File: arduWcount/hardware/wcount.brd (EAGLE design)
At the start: 100 x 80 mm, 25 parts, among them IC1 MEGA8-AI, Q2 BC447, Q4 BC447

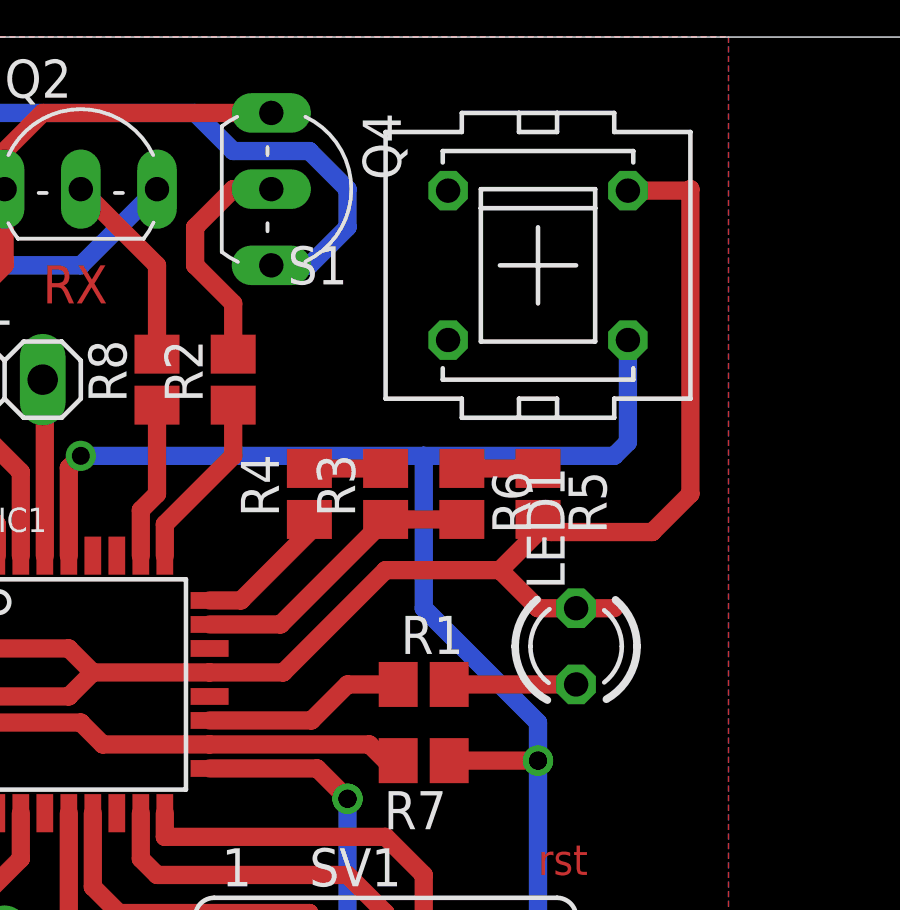
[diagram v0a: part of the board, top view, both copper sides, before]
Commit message: EEPROM rotating added
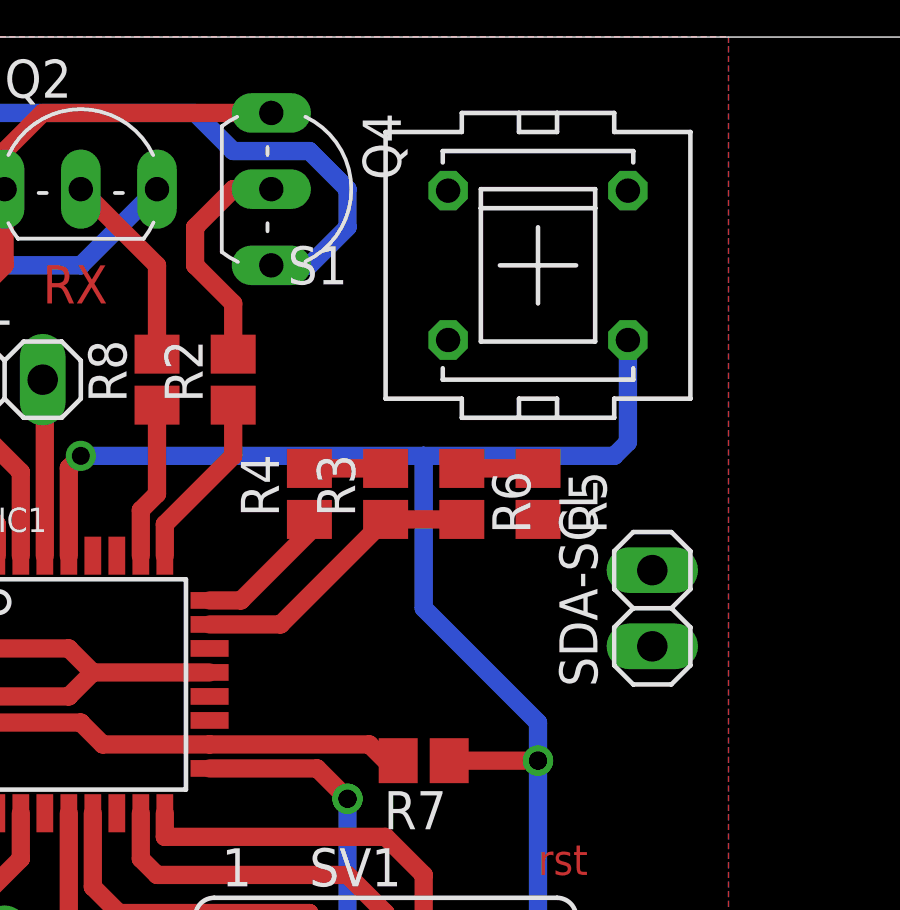
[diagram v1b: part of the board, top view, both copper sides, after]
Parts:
- removed LED1: (no value), led:LED3MM
- removed R1: (no value), resistor:R0805
- added SDA-SCL: (no value), pinhead:1X02
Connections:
- net GNDA: no longer LED1.K
- net N$22: now also IC1.27, SDA-SCL.1; no longer LED1.A, R1.2
- net N$23: now also IC1.28, SDA-SCL.2; no longer IC1.19, R1.1
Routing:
- net GNDA: track 151.3 -> 116.1 mm
- net N$23: track 6.78 -> 0.00 mm
- net N$22: track 4.23 -> 0.00 mm
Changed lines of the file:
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@@
 <attribute name="SPICEPREFIX" value="C" x="-13.97" y="116.84" size="1.778" layer="27" rot="R180" display="off"/>
 </element>
-<element name="LED1" library="led" package="LED3MM" value="" x="39.37" y="59.69" rot="R90"/>
-<element name="R1" library="resistor" package="R0805" value="" x="34.29" y="58.42"/>
 <element name="R5" library="resistor" package="R0805" value="" x="38.1" y="64.77" rot="R270"/>
 <element name="R6" library="resistor" package="R0805" value="" x="35.56" y="64.77" rot="R270"/>
@@
 </element>
 <element name="C5" library="resistor" package="C0805" value="0.1 mf" x="40.64" y="48.26" rot="R270"/>
+<element name="SDA-SCL" library="pinhead" package="1X02" value="" x="41.91" y="60.96" rot="R90"/>
 </elements>
 <signals>
@@
 <via x="38.1" y="55.88" extent="1-16" drill="0.6" diameter="0.8128"/>
 <contactref element="C5" pad="1"/>
-<wire x1="22.86" y1="66.04" x2="22.86" y2="66.04" width="0" layer="19" extent="1-16"/>
 <wire x1="38.1" y1="49.53" x2="40.64" y2="49.53" width="0.6096" layer="1"/>
 <wire x1="40.64" y1="49.53" x2="40.64" y2="49.11" width="0.6096" layer="1"/>
-</signal>
-<signal name="N$22">
-<contactref element="LED1" pad="A"/>
-<contactref element="R1" pad="2"/>
-<wire x1="35.14" y1="58.42" x2="39.37" y2="58.42" width="0.6096" layer="1"/>
-</signal>
-<signal name="N$23">
-<contactref element="IC1" pad="19"/>
-<contactref element="R1" pad="1"/>
-<wire x1="27.1526" y1="57.22" x2="30.55" y2="57.22" width="0.6096" layer="1"/>
-<wire x1="30.55" y1="57.22" x2="31.75" y2="58.42" width="0.6096" layer="1"/>
-<wire x1="31.75" y1="58.42" x2="33.44" y2="58.42" width="0.6096" layer="1"/>
+<wire x1="22.86" y1="66.04" x2="22.86" y2="66.04" width="0" layer="19" extent="1-16"/>
 </signal>
 <signal name="N$25">
@@
 <contactref element="SV1" pad="2"/>
 <contactref element="R5" pad="2"/>
-<contactref element="LED1" pad="K"/>
 <contactref element="VALTEC" pad="2"/>
 <contactref element="PWR" pad="1"/>
@@
 <wire x1="23.26" y1="58.82" x2="22.46" y2="58.02" width="0.6096" layer="1"/>
 <wire x1="22.46" y1="58.02" x2="18.5674" y2="58.02" width="0.6096" layer="1"/>
-<wire x1="27.1526" y1="58.82" x2="29.61" y2="58.82" width="0.6096" layer="1"/>
-<wire x1="29.61" y1="58.82" x2="33.02" y2="62.23" width="0.6096" layer="1"/>
-<wire x1="33.02" y1="62.23" x2="36.83" y2="62.23" width="0.6096" layer="1"/>
-<wire x1="36.83" y1="62.23" x2="38.1" y2="63.5" width="0.6096" layer="1"/>
-<wire x1="39.37" y1="60.96" x2="38.1" y2="60.96" width="0.6096" layer="1"/>
-<wire x1="38.1" y1="60.96" x2="36.83" y2="62.23" width="0.6096" layer="1"/>
 <wire x1="20.32" y1="49.53" x2="20.32" y2="46.99" width="0.6096" layer="1"/>
 <wire x1="20.32" y1="46.99" x2="2.54" y2="46.99" width="0.6096" layer="1"/>
@@
 <wire x1="2.54" y1="50.48" x2="2.86" y2="50.8" width="0.6096" layer="1"/>
 <wire x1="27.94" y1="46.99" x2="20.32" y2="46.99" width="0.6096" layer="1"/>
-<wire x1="41.0972" y1="74.8792" x2="43.1292" y2="74.8792" width="0.6096" layer="1"/>
-<wire x1="43.1292" y1="74.8792" x2="43.18" y2="74.93" width="0.6096" layer="1"/>
-<wire x1="43.18" y1="74.93" x2="43.18" y2="64.77" width="0.6096" layer="1"/>
-<wire x1="43.18" y1="64.77" x2="41.91" y2="63.5" width="0.6096" layer="1"/>
-<wire x1="41.91" y1="63.5" x2="38.52" y2="63.5" width="0.6096" layer="1"/>
-<wire x1="38.52" y1="63.5" x2="38.1" y2="63.92" width="0.6096" layer="1"/>
 <wire x1="2.54" y1="59.69" x2="1.27" y2="60.96" width="0.6096" layer="1"/>
 <wire x1="1.27" y1="60.96" x2="1.27" y2="67.31" width="0.6096" layer="1"/>
@@
 <wire x1="18.5674" y1="59.62" x2="22.46" y2="59.62" width="0.6096" layer="1"/>
 <wire x1="22.46" y1="59.62" x2="23.26" y2="58.82" width="0.6096" layer="1"/>
-<wire x1="39.37" y1="60.96" x2="40.64" y2="60.96" width="0.6096" layer="1"/>
 <polygon width="0.6096" layer="1" isolate="0.8128">
 <vertex x="0" y="80.01"/>
@@
 <vertex x="0" y="41.91"/>
 </polygon>
+<wire x1="41.0972" y1="74.8792" x2="38.1" y2="63.92" width="0" layer="19" extent="1-1"/>
+<wire x1="27.1526" y1="58.82" x2="38.1" y2="63.92" width="0" layer="19" extent="1-1"/>
 </signal>
 <signal name="N$16">
@@
 <wire x1="38.1" y1="47.41" x2="38.1" y2="46.99" width="0.6096" layer="1"/>
 </signal>
+<signal name="N$22">
+<contactref element="IC1" pad="27"/>
+<contactref element="SDA-SCL" pad="1"/>
+<wire x1="24.06" y1="62.7126" x2="41.91" y2="59.69" width="0" layer="19" extent="1-1"/>
+</signal>
+<signal name="N$23">
+<contactref element="IC1" pad="28"/>
+<contactref element="SDA-SCL" pad="2"/>
+<wire x1="23.26" y1="62.7126" x2="41.91" y2="62.23" width="0" layer="19" extent="1-1"/>
+</signal>
 </signals>
